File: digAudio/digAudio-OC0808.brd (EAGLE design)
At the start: 18.8 x 21.5 mm, 12 parts, among them IC1 DIT4096-H

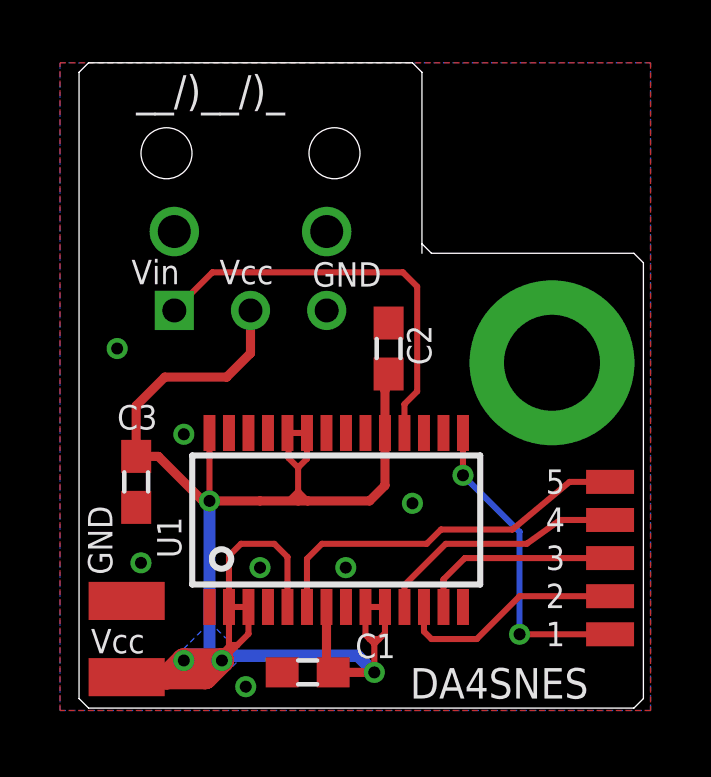
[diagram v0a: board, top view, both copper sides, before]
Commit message: bugfix on PCBs: - pin 14 (M/nS) was floating - now it is properly connected to GND
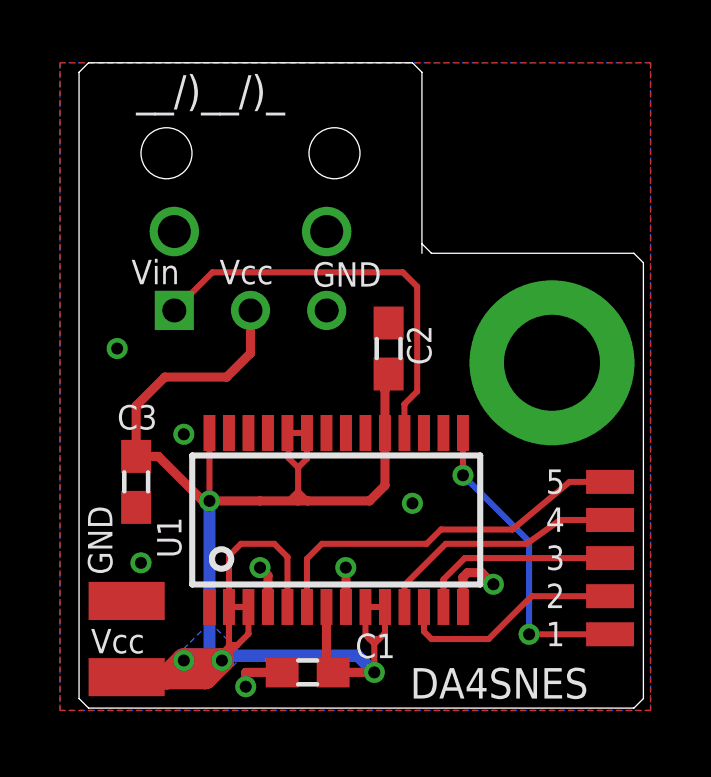
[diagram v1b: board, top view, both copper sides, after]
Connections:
- net GND: now also IC1.14
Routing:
- net GND: track 0.00 -> 6.66 mm, vias 8 -> 9
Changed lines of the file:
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@@
 <?xml version="1.0" encoding="utf-8"?>
 <!DOCTYPE eagle SYSTEM "eagle.dtd">
-<eagle version="8.6.0">
+<eagle version="9.6.2">
 <drawing>
 <settings>
@@
 <param name="checkStop" value="0"/>
 <param name="checkValues" value="0"/>
+<param name="checkNames" value="1"/>
+<param name="checkWireStubs" value="1"/>
+<param name="checkPolygonWidth" value="0"/>
 <param name="useDiameter" value="13"/>
 <param name="maxErrors" value="50"/>
@@
 <element name="3" library="wirepad" package="SMD0,8-1,6" value="" x="18.335625" y="5.08" smashed="yes" rot="R90"/>
 <element name="1" library="wirepad" package="SMD0,8-1,6" value="" x="18.335625" y="2.54" smashed="yes" rot="R90"/>
-<element name="U$1" library="cs8406" package="JT_OC-0808T*008" value="JT_OC0808" x="6.35" y="13.335" rot="MR0"/>
+<element name="U$1" library="cs8406" package="JT_OC-0808T*008" value="JT_OC0808" x="6.35" y="13.335" smashed="yes" rot="MR0"/>
 </elements>
 <signals>
@@
 <contactref element="U$1" pad="P$3"/>
 <via x="6.19125" y="0.79375" extent="1-16" drill="0.4"/>
+<contactref element="IC1" pad="14"/>
+<via x="14.44625" y="4.206875" extent="1-16" drill="0.4"/>
+<wire x1="13.4325" y1="3.45" x2="13.4325" y2="4.4440125" width="0.3048" layer="1"/>
+<wire x1="13.4325" y1="4.4440125" x2="13.58268125" y2="4.59419375" width="0.3048" layer="1"/>
+<wire x1="13.58268125" y1="4.59419375" x2="14.05893125" y2="4.59419375" width="0.3048" layer="1"/>
+<wire x1="14.05893125" y1="4.59419375" x2="14.44625" y2="4.206875" width="0.3048" layer="1"/>
+<wire x1="9.5325" y1="3.45" x2="9.5325" y2="4.755" width="0.3048" layer="1"/>
+<wire x1="9.5325" y1="4.755" x2="9.525" y2="4.7625" width="0.3048" layer="1"/>
+<wire x1="6.9325" y1="3.45" x2="6.9325" y2="4.4975" width="0.3048" layer="1"/>
+<wire x1="6.9325" y1="4.4975" x2="6.6675" y2="4.7625" width="0.3048" layer="1"/>
+<wire x1="6.19125" y1="0.79375" x2="6.19125" y2="1.27" width="0.3048" layer="1"/>
+<wire x1="6.19125" y1="1.27" x2="7.405" y2="1.27" width="0.3048" layer="1"/>
 </signal>
 <signal name="VCC">
@@
 <contactref element="IC1" pad="15"/>
 <contactref element="1" pad="P$1"/>
-<wire x1="18.335625" y1="2.54" x2="15.319375" y2="2.54" width="0.2032" layer="1"/>
-<via x="15.319375" y="2.54" extent="1-16" drill="0.4"/>
-<wire x1="15.319375" y1="2.54" x2="15.319375" y2="5.953125" width="0.2032" layer="16"/>
-<wire x1="15.319375" y1="5.953125" x2="13.4325" y2="7.84" width="0.2032" layer="16"/>
+<wire x1="18.335625" y1="2.54" x2="15.636875" y2="2.54" width="0.2032" layer="1"/>
+<via x="15.636875" y="2.54" extent="1-16" drill="0.4"/>
+<wire x1="15.636875" y1="2.54" x2="15.636875" y2="5.635625" width="0.2032" layer="16"/>
+<wire x1="15.636875" y1="5.635625" x2="13.4325" y2="7.84" width="0.2032" layer="16"/>
 <via x="13.4325" y="7.84" extent="1-16" drill="0.4"/>
 <wire x1="13.4325" y1="9.25" x2="13.4325" y2="7.84" width="0.2032" layer="1"/>
@@
 <wire x1="12.1325" y1="3.45" x2="12.1325" y2="2.63125" width="0.2032" layer="1"/>
 <wire x1="12.1325" y1="2.63125" x2="12.3825" y2="2.38125" width="0.2032" layer="1"/>
-<wire x1="12.3825" y1="2.38125" x2="13.890625" y2="2.38125" width="0.2032" layer="1"/>
-<wire x1="13.890625" y1="2.38125" x2="15.319375" y2="3.81" width="0.2032" layer="1"/>
-<wire x1="15.319375" y1="3.81" x2="18.335625" y2="3.81" width="0.2032" layer="1"/>
+<wire x1="12.3825" y1="2.38125" x2="14.2875" y2="2.38125" width="0.2032" layer="1"/>
+<wire x1="14.2875" y1="2.38125" x2="15.71625" y2="3.81" width="0.2032" layer="1"/>
+<wire x1="15.71625" y1="3.81" x2="18.335625" y2="3.81" width="0.2032" layer="1"/>
 </signal>
 <signal name="N$6">
@@
 </signal>
 </signals>
+<mfgpreviewcolors>
+<mfgpreviewcolor name="soldermaskcolor" color="0xC8008000"/>
+<mfgpreviewcolor name="silkscreencolor" color="0xFFFEFEFE"/>
+<mfgpreviewcolor name="backgroundcolor" color="0xFF282828"/>
+<mfgpreviewcolor name="coppercolor" color="0xFFFFBF00"/>
+<mfgpreviewcolor name="substratecolor" color="0xFF786E46"/>
+</mfgpreviewcolors>
 </board>
 </drawing>
